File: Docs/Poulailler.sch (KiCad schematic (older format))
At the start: 36 parts, among them Q1 Q_PNP_ECB

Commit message: Add reset & test switches
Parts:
- removed D? (x4): D, symbol D
- added D?: LED, symbol LED
- added R?: 1K, symbol R
- added SW?: Test, symbol SW_PUSH
- added SW?: Prog, symbol SW_PUSH
- added U?: Reg 3.3, SOT-23, symbol APE8865NR-33-HF-3
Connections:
- net labels added: +5V
- wire segments 109 -> 108
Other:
- moved on the sheet: 5V
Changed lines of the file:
@@
 LIBS:contrib
 LIBS:valves
+LIBS:device
 LIBS:Poulailler-cache
 EELAYER 25 0
@@
 L Battery 5V
 U 1 1 5A249A56
-P 9200 1100
-F 0 "5V" V 9350 1050 50  0000 L CNN
-F 1 "Power Bank" V 9050 900 50  0000 L CNN
-F 2 "" V 9200 1160 50  0001 C CNN
-F 3 "" V 9200 1160 50  0001 C CNN
-	1    9200 1100
+P 9200 1000
+F 0 "5V" V 9350 950 50  0000 L CNN
+F 1 "Power Bank" V 9050 800 50  0000 L CNN
+F 2 "" V 9200 1060 50  0001 C CNN
+F 3 "" V 9200 1060 50  0001 C CNN
+	1    9200 1000
 	0    -1   -1   0
-$EndComp
-$Comp
-L D D?
-U 1 1 5A249B94
-P 8700 950
-F 0 "D?" H 8700 1050 50  0001 C CNN
-F 1 "D" H 8700 850 50  0001 C CNN
-F 2 "" H 8700 950 50  0001 C CNN
-F 3 "" H 8700 950 50  0001 C CNN
-	1    8700 950
-	0    -1   -1   0
-$EndComp
-$Comp
-L D D?
-U 1 1 5A249C13
-P 8850 950
-F 0 "D?" H 8850 1050 50  0001 C CNN
-F 1 "D" H 8850 850 50  0001 C CNN
-F 2 "" H 8850 950 50  0001 C CNN
-F 3 "" H 8850 950 50  0001 C CNN
-	1    8850 950
-	0    -1   1    0
-$EndComp
-$Comp
-L D D?
-U 1 1 5A249C42
-P 8550 950
-F 0 "D?" H 8550 1050 50  0001 C CNN
-F 1 "D" H 8550 850 50  0001 C CNN
-F 2 "" H 8550 950 50  0001 C CNN
-F 3 "" H 8550 950 50  0001 C CNN
-	1    8550 950
-	0    -1   1    0
 $EndComp
 $Comp
@@
 	1    0    0    -1
 $EndComp
-Text GLabel 7750 1000 0    60   Input ~ 0
-+3,3
 $Comp
 L D D?
 U 1 1 5A24B677
-P 8100 1150
-F 0 "D?" H 8100 1250 50  0001 C CNN
-F 1 "Dd" H 8100 1050 50  0000 C CNN
-F 2 "" H 8100 1150 50  0001 C CNN
-F 3 "" H 8100 1150 50  0001 C CNN
-	1    8100 1150
-	0    1    -1   0
-$EndComp
-$Comp
-L D D?
-U 1 1 5A24B69A
-P 8250 1300
-F 0 "D?" H 8250 1400 50  0001 C CNN
-F 1 "D" H 8250 1200 50  0001 C CNN
-F 2 "" H 8250 1300 50  0001 C CNN
-F 3 "" H 8250 1300 50  0001 C CNN
-	1    8250 1300
-	-1   0    0    -1
+P 8200 3300
+F 0 "D?" H 8200 3400 50  0001 C CNN
+F 1 "Dd" H 8200 3200 50  0000 C CNN
+F 2 "" H 8200 3300 50  0001 C CNN
+F 3 "" H 8200 3300 50  0001 C CNN
+	1    8200 3300
+	0    1    1    0
 $EndComp
 $Comp
@@
 Text GLabel 9350 3350 1    60   Input ~ 0
 +3,3
+$Comp
+L R R?
+U 1 1 5A46A837
+P 3300 1950
+F 0 "R?" V 3380 1950 50  0001 C CNN
+F 1 "10k" V 3300 1950 50  0000 C CNN
+F 2 "" V 3230 1950 50  0001 C CNN
+F 3 "" H 3300 1950 50  0001 C CNN
+	1    3300 1950
+	1    0    0    -1
+$EndComp
+$Comp
+L APE8865NR-33-HF-3 U?
+U 1 1 5A479B76
+P 8350 1050
+F 0 "U?" H 8050 1300 50  0001 C CNN
+F 1 "Reg 3.3" H 8350 1250 50  0000 C CNN
+F 2 "SOT-23" H 8350 1150 50  0001 C CIN
+F 3 "" H 8350 1050 50  0000 C CNN
+	1    8350 1050
+	-1   0    0    -1
+$EndComp
+Text GLabel 9000 800  1    60   Input ~ 0
++5V
+$Comp
+L R R?
+U 1 1 5A47A843
+P 3500 1800
+F 0 "R?" V 3580 1800 50  0001 C CNN
+F 1 "1K" V 3500 1800 50  0000 C CNN
+F 2 "" V 3430 1800 50  0001 C CNN
+F 3 "" H 3500 1800 50  0001 C CNN
+	1    3500 1800
+	1    0    0    -1
+$EndComp
+$Comp
+L LED D?
+U 1 1 5A47AA84
+P 3500 1450
+F 0 "D?" H 3500 1550 50  0001 C CNN
+F 1 "LED" H 3500 1350 50  0001 C CNN
+F 2 "" H 3500 1450 50  0000 C CNN
+F 3 "" H 3500 1450 50  0000 C CNN
+	1    3500 1450
+	0    -1   -1   0
+$EndComp
+$Comp
+L SW_PUSH SW?
+U 1 1 5A47AB6F
+P 3750 1800
+F 0 "SW?" H 3900 1910 50  0001 C CNN
+F 1 "Test" H 3750 1720 50  0000 C CNN
+F 2 "" H 3750 1800 50  0000 C CNN
+F 3 "" H 3750 1800 50  0000 C CNN
+	1    3750 1800
+	0    -1   -1   0
+$EndComp
 Wire Wire Line
 	8000 2450 8100 2450
@@
 Connection ~ 5400 2150
 Wire Wire Line
-	8000 2950 8000 3400
+	8000 2950 8000 3450
 Wire Wire Line
 	5350 2050 5700 2050
@@
 Wire Wire Line
 	4250 1400 4250 1200
-Wire Wire Line
-	2900 1450 4350 1450
-Wire Wire Line
-	4350 1450 4350 1200
 Wire Wire Line
 	3600 2300 4950 2300
@@
 	4350 3050 650  3050
 Wire Wire Line
-	2900 2000 2900 1450
+	2900 1250 2900 2000
 Wire Wire Line
 	2150 1900 2900 1900
@@
 Wire Wire Line
 	9850 1800 9850 1850
-Wire Wire Line
-	8850 1100 9000 1100
 Connection ~ 9600 3050
-Wire Wire Line
-	8700 800  8850 800
-Wire Wire Line
-	8700 1100 8550 1100
-Wire Wire Line
-	9400 1100 9600 1100
 Connection ~ 9600 1600
 Wire Wire Line
 	9000 1500 9850 1500
 Wire Wire Line
-	7750 1000 8400 1000
-Wire Wire Line
-	8400 1000 8400 800
-Wire Wire Line
-	8400 800  8550 800
-Wire Wire Line
-	9000 1100 9000 1500
-Wire Wire Line
-	9600 1100 9600 4000
+	9000 800  9000 1500
+Wire Wire Line
+	9600 1000 9600 4000
 Wire Wire Line
 	8700 2050 8700 3050
 Connection ~ 8700 3050
 Wire Wire Line
-	8000 2550 8750 2550
-Wire Wire Line
-	8400 1300 8750 1300
-Wire Wire Line
-	8750 1300 8750 2550
-Wire Wire Line
 	8000 2850 8450 2850
 Wire Wire Line
@@
 	4700 1150 4700 1250
 Wire Wire Line
-	4700 1250 4350 1250
-Connection ~ 4350 1250
-Wire Wire Line
-	5050 1050 5850 1050
+	5050 1050 7900 1050
 Wire Wire Line
 	5850 1050 5850 1150
 Connection ~ 5050 1050
-$Comp
-L R R?
-U 1 1 5A46A837
-P 3350 1950
-F 0 "R?" V 3430 1950 50  0001 C CNN
-F 1 "10k" V 3350 1950 50  0000 C CNN
-F 2 "" V 3280 1950 50  0001 C CNN
-F 3 "" H 3350 1950 50  0001 C CNN
-	1    3350 1950
-	1    0    0    -1
-$EndComp
-Wire Wire Line
-	3350 1450 3350 1800
-Connection ~ 3350 1450
-Wire Wire Line
-	3350 2100 4000 2100
-Connection ~ 3350 2100
-Wire Wire Line
-	3300 2300 3350 2300
-Wire Wire Line
-	3350 2300 3350 2100
+Wire Wire Line
+	3300 1250 3300 1800
+Wire Wire Line
+	8000 3450 8200 3450
+Connection ~ 8000 3400
+Wire Wire Line
+	8200 3150 8200 2550
+Wire Wire Line
+	8200 2550 8000 2550
+Wire Wire Line
+	9400 1000 9600 1000
+Wire Wire Line
+	9000 1000 8800 1000
+Wire Wire Line
+	8350 1350 9600 1350
+Connection ~ 9600 1350
+Wire Wire Line
+	7900 1050 7900 1000
+Connection ~ 5850 1050
+Connection ~ 9000 1000
+Wire Wire Line
+	3300 2100 4000 2100
+Wire Wire Line
+	3300 2100 3300 2300
+Wire Wire Line
+	4350 1200 4350 1250
+Wire Wire Line
+	4700 1250 2900 1250
+Connection ~ 3300 1250
+Connection ~ 3500 1250
+Connection ~ 3750 2100
+Wire Wire Line
+	3750 1500 3600 1500
+Wire Wire Line
+	3600 1500 3600 1950
+Wire Wire Line
+	3600 1950 3500 1950
+Connection ~ 4350 1250
+$Comp
+L SW_PUSH SW?
+U 1 1 5A47B2D3
+P 5250 3200
+F 0 "SW?" H 5400 3310 50  0001 C CNN
+F 1 "Prog" H 5250 3120 50  0000 C CNN
+F 2 "" H 5250 3200 50  0000 C CNN
+F 3 "" H 5250 3200 50  0000 C CNN
+	1    5250 3200
+	1    0    0    -1
+$EndComp
+Wire Wire Line
+	5550 3200 5550 2050
+Connection ~ 5550 2050
 $EndSCHEMATC

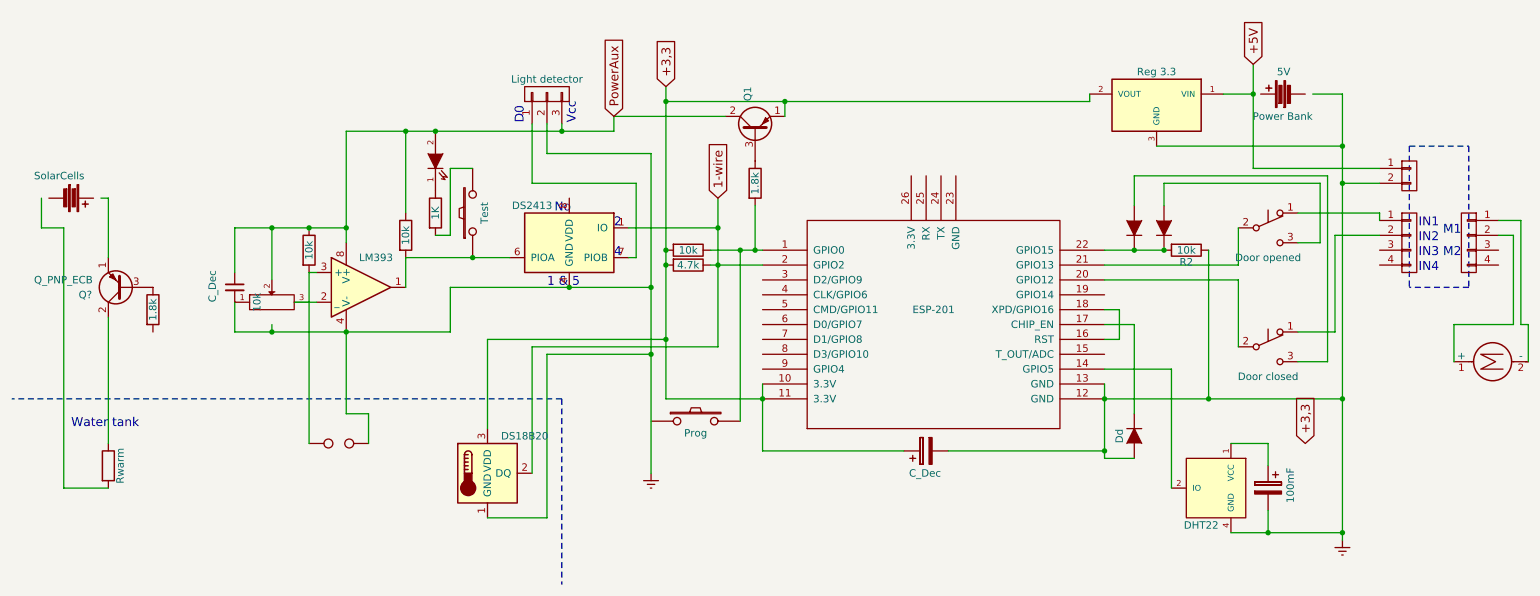
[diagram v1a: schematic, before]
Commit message: Invert PIO.A & PIO.B
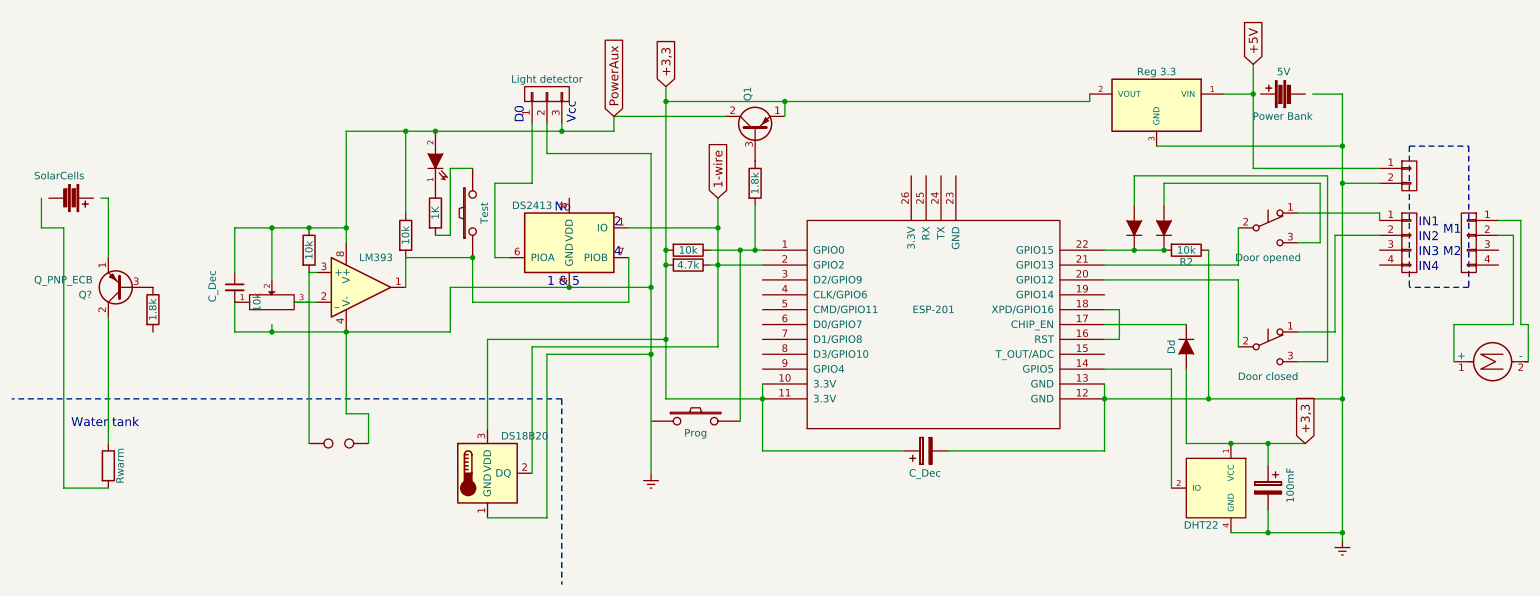
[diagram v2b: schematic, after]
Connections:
- wire segments 108 -> 110
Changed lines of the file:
@@
 L D D?
 U 1 1 5A24B677
-P 8200 3300
-F 0 "D?" H 8200 3400 50  0001 C CNN
-F 1 "Dd" H 8200 3200 50  0000 C CNN
-F 2 "" H 8200 3300 50  0001 C CNN
-F 3 "" H 8200 3300 50  0001 C CNN
-	1    8200 3300
+P 8550 2700
+F 0 "D?" H 8550 2800 50  0001 C CNN
+F 1 "Dd" H 8550 2600 50  0000 C CNN
+F 2 "" H 8550 2700 50  0001 C CNN
+F 3 "" H 8550 2700 50  0001 C CNN
+	1    8550 2700
 	0    1    1    0
 $EndComp
@@
 F 3 "" H 9100 3650 50  0001 C CNN
 	1    9100 3650
-	-1   0    0    -1
-$EndComp
-$Comp
-L DS28EA00 U?
-U 1 1 5A233EEF
-P 4400 2000
-F 0 "U?" H 4150 2250 50  0001 C CNN
-F 1 "DS2413" H 4650 2250 50  0000 C CNN
-F 2 "Housings_SSOP:MSOP-8_3x3mm_Pitch0.65mm" H 3400 1750 50  0001 C CNN
-F 3 "" H 4150 2250 50  0001 C CNN
-	1    4400 2000
 	-1   0    0    -1
 $EndComp
@@
 Connection ~ 5400 2150
 Wire Wire Line
-	8000 2950 8000 3450
-Wire Wire Line
 	5350 2050 5700 2050
 Connection ~ 5400 1900
@@
 Wire Wire Line
 	4150 1200 4150 1600
-Wire Wire Line
-	4150 1600 4850 1600
-Wire Wire Line
-	4850 1600 4850 2100
-Wire Wire Line
-	4850 2100 4800 2100
 Wire Wire Line
 	4950 1400 4250 1400
@@
 Connection ~ 9100 3950
 Wire Wire Line
-	9100 3500 9100 3350
-Wire Wire Line
-	9100 3350 8850 3350
+	9100 3350 9100 3500
+Wire Wire Line
+	8550 3350 9350 3350
 Wire Wire Line
 	5400 1700 5400 2700
@@
 	3300 1250 3300 1800
 Wire Wire Line
-	8000 3450 8200 3450
-Connection ~ 8000 3400
-Wire Wire Line
-	8200 3150 8200 2550
-Wire Wire Line
-	8200 2550 8000 2550
+	8000 2550 8550 2550
 Wire Wire Line
 	9400 1000 9600 1000
@@
 Connection ~ 5850 1050
 Connection ~ 9000 1000
-Wire Wire Line
-	3300 2100 4000 2100
 Wire Wire Line
 	3300 2100 3300 2300
@@
 	5550 3200 5550 2050
 Connection ~ 5550 2050
+Wire Wire Line
+	8000 2950 8000 3400
+Wire Wire Line
+	8550 2850 8550 3350
+Connection ~ 8850 3350
+Connection ~ 9100 3350
+$Comp
+L DS28EA00 U?
+U 1 1 5A233EEF
+P 4400 2000
+F 0 "U?" H 4150 2250 50  0001 C CNN
+F 1 "DS2413" H 4650 2250 50  0000 C CNN
+F 2 "Housings_SSOP:MSOP-8_3x3mm_Pitch0.65mm" H 3400 1750 50  0001 C CNN
+F 3 "" H 4150 2250 50  0001 C CNN
+	1    4400 2000
+	-1   0    0    -1
+$EndComp
+Wire Wire Line
+	3300 2100 3750 2100
+Wire Wire Line
+	3750 2100 3750 2400
+Wire Wire Line
+	3750 2400 4800 2400
+Wire Wire Line
+	4800 2400 4800 2100
+Wire Wire Line
+	4150 1600 3900 1600
+Wire Wire Line
+	3900 1600 3900 2100
+Wire Wire Line
+	3900 2100 4000 2100
 $EndSCHEMATC

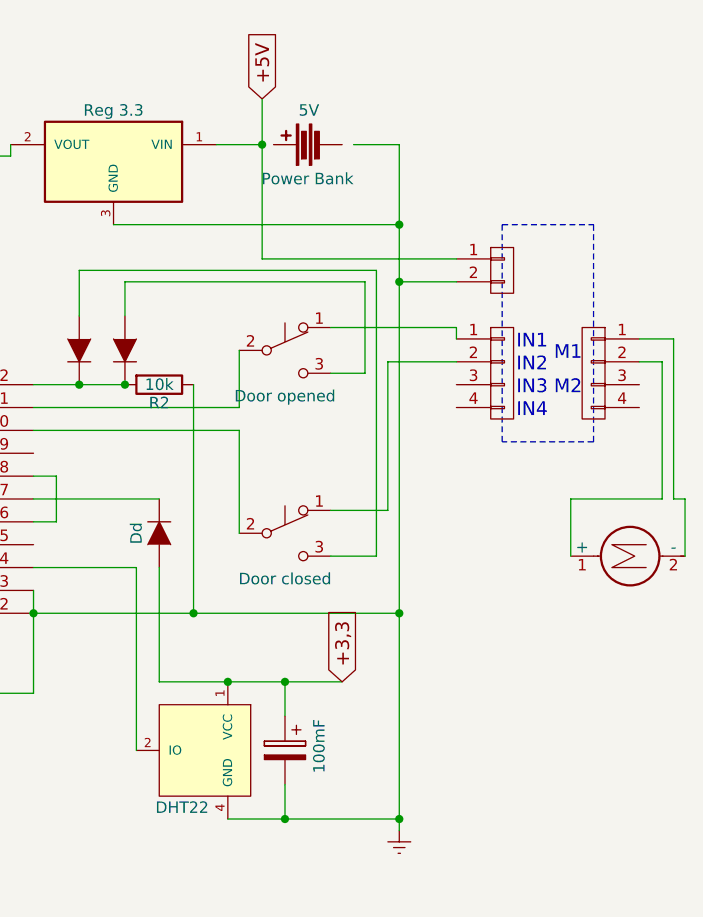
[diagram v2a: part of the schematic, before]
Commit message: Add a power switch
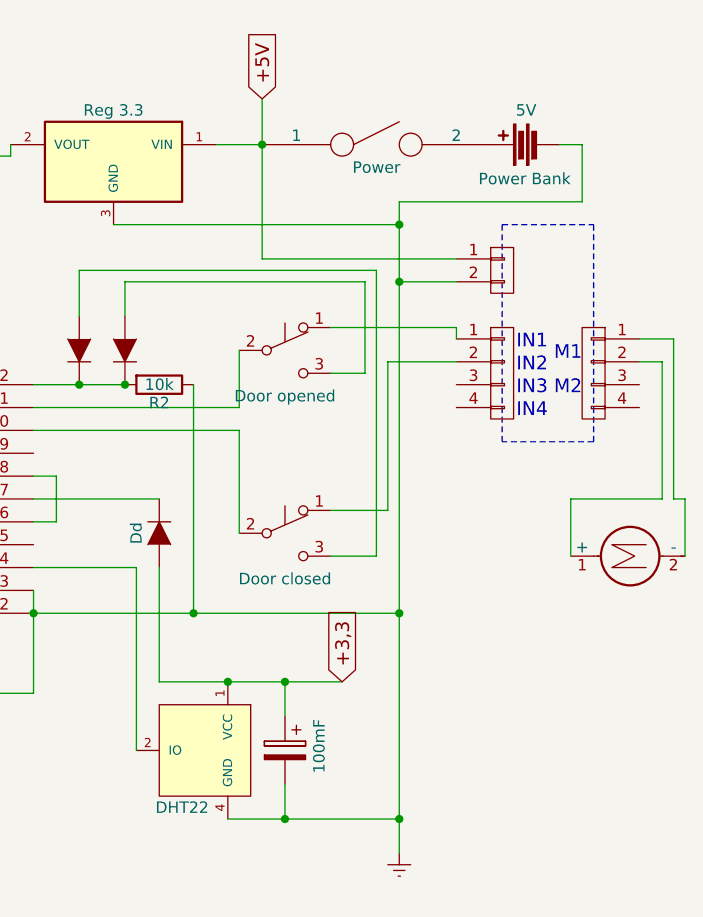
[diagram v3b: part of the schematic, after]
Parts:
- added SW?: Power, symbol SPST
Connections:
- wire segments 110 -> 112
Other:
- moved on the sheet: 5V
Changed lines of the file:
@@
 L Battery 5V
 U 1 1 5A249A56
-P 9200 1000
-F 0 "5V" V 9350 950 50  0000 L CNN
-F 1 "Power Bank" V 9050 800 50  0000 L CNN
-F 2 "" V 9200 1060 50  0001 C CNN
-F 3 "" V 9200 1060 50  0001 C CNN
-	1    9200 1000
+P 10150 1000
+F 0 "5V" V 10300 950 50  0000 L CNN
+F 1 "Power Bank" V 10000 800 50  0000 L CNN
+F 2 "" V 10150 1060 50  0001 C CNN
+F 3 "" V 10150 1060 50  0001 C CNN
+	1    10150 1000
 	0    -1   -1   0
 $EndComp
@@
 L Earth #PWR?
 U 1 1 5A249F46
-P 9600 4000
-F 0 "#PWR?" H 9600 3750 50  0001 C CNN
-F 1 "Earth" H 9600 3850 50  0001 C CNN
-F 2 "" H 9600 4000 50  0001 C CNN
-F 3 "" H 9600 4000 50  0001 C CNN
-	1    9600 4000
+P 9600 4100
+F 0 "#PWR?" H 9600 3850 50  0001 C CNN
+F 1 "Earth" H 9600 3950 50  0001 C CNN
+F 2 "" H 9600 4100 50  0001 C CNN
+F 3 "" H 9600 4100 50  0001 C CNN
+	1    9600 4100
 	1    0    0    -1
 $EndComp
@@
 	9000 800  9000 1500
 Wire Wire Line
-	9600 1000 9600 4000
-Wire Wire Line
 	8700 2050 8700 3050
 Connection ~ 8700 3050
@@
 	8450 2850 8450 3650
 Wire Wire Line
-	8850 3950 9600 3950
+	9600 3950 8850 3950
 Connection ~ 9600 3950
 Wire Wire Line
@@
 Wire Wire Line
 	8000 2550 8550 2550
-Wire Wire Line
-	9400 1000 9600 1000
 Wire Wire Line
 	9000 1000 8800 1000
@@
 Wire Wire Line
 	3900 2100 4000 2100
+$Comp
+L SPST SW?
+U 1 1 5A4B95FD
+P 9500 1000
+F 0 "SW?" H 9500 1100 50  0001 C CNN
+F 1 "Power" H 9500 900 50  0000 C CNN
+F 2 "" H 9500 1000 50  0000 C CNN
+F 3 "" H 9500 1000 50  0000 C CNN
+	1    9500 1000
+	1    0    0    -1
+$EndComp
+Wire Wire Line
+	9600 1250 9600 4100
+Wire Wire Line
+	9600 1250 10400 1250
+Wire Wire Line
+	10400 1250 10400 1000
+Wire Wire Line
+	10400 1000 10300 1000
 $EndSCHEMATC
